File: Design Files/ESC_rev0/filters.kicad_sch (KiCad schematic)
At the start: 0 parts

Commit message: update 9
filters and USB complete
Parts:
- added C49, C50, C52, C54: 100n, symbol Device:C
- added C51, C53, C55, C58: 4n7, symbol Device:C
- added J9: Conn_01x06, symbol Connector_Generic:Conn_01x06
- added R45, R47, R49, R50: 10k, symbol Device:R
- added R46, R48, R52: 2k2, symbol Device:R
- added R51: 0R, symbol Device:R
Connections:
- new net +3.3V: C49.1, C50.1, C52.1, C54.1, R46.1, R48.1, R50.1, R52.1
- new net +5V: J9.6 (Pin_6)
- new net GND: C49.2, C50.2, C51.2, C52.2, C53.2, C54.2, C55.2, C58.2, J9.1 (Pin_1)
- new net HALL_1_IN: C58.1, J9.4 (Pin_4), R45.1, R52.2
- new net HALL_2_IN: C53.1, J9.3 (Pin_3), R48.2, R49.1
- new net HALL_3_IN: C51.1, J9.2 (Pin_2), R46.2, R47.1
- new net HALL_3_OUT: R45.2, R47.2, R49.2, R51.2
- new net TEMP_IN: C55.1, J9.5 (Pin_5), R50.2, R51.1
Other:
- note added: "${TITLE}"
- note added: "HALL_1 Filter"
- note added: "HALL_2 Filter"
- note added: "HALL_3 Filter"
- note added: "Hall Encoder Input"
- note added: "Hall Encoder Output to MCU"
- note added: "TEMP Filter"
- title: (none) -> FILTERS

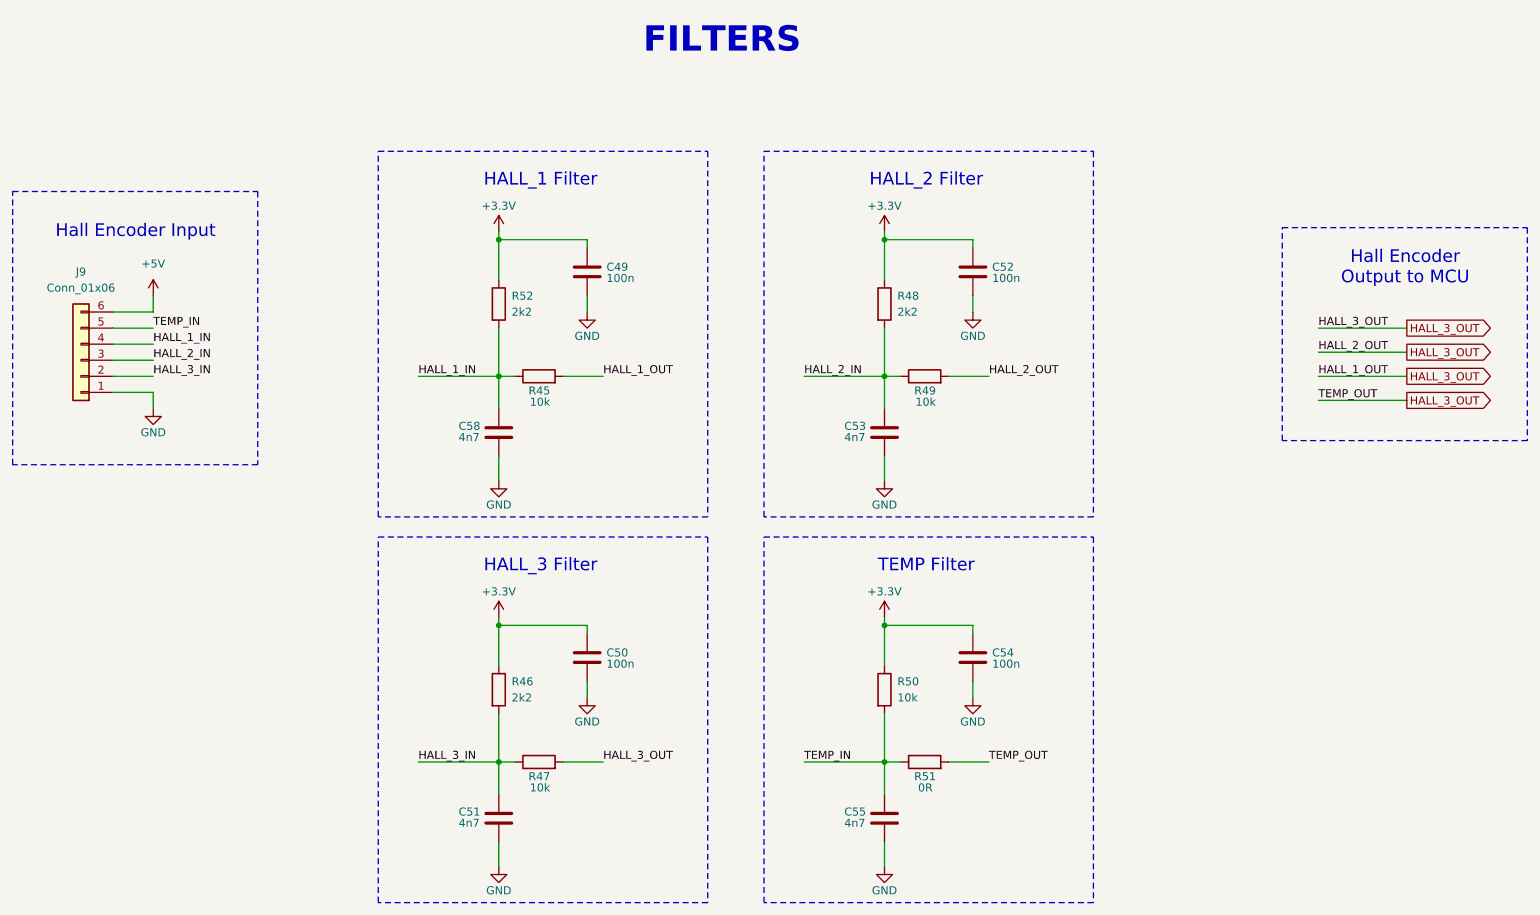
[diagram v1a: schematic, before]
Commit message: UPDATE 12
started schematics revision: edit and added info and circuits to some pages and assigned some footprints for components
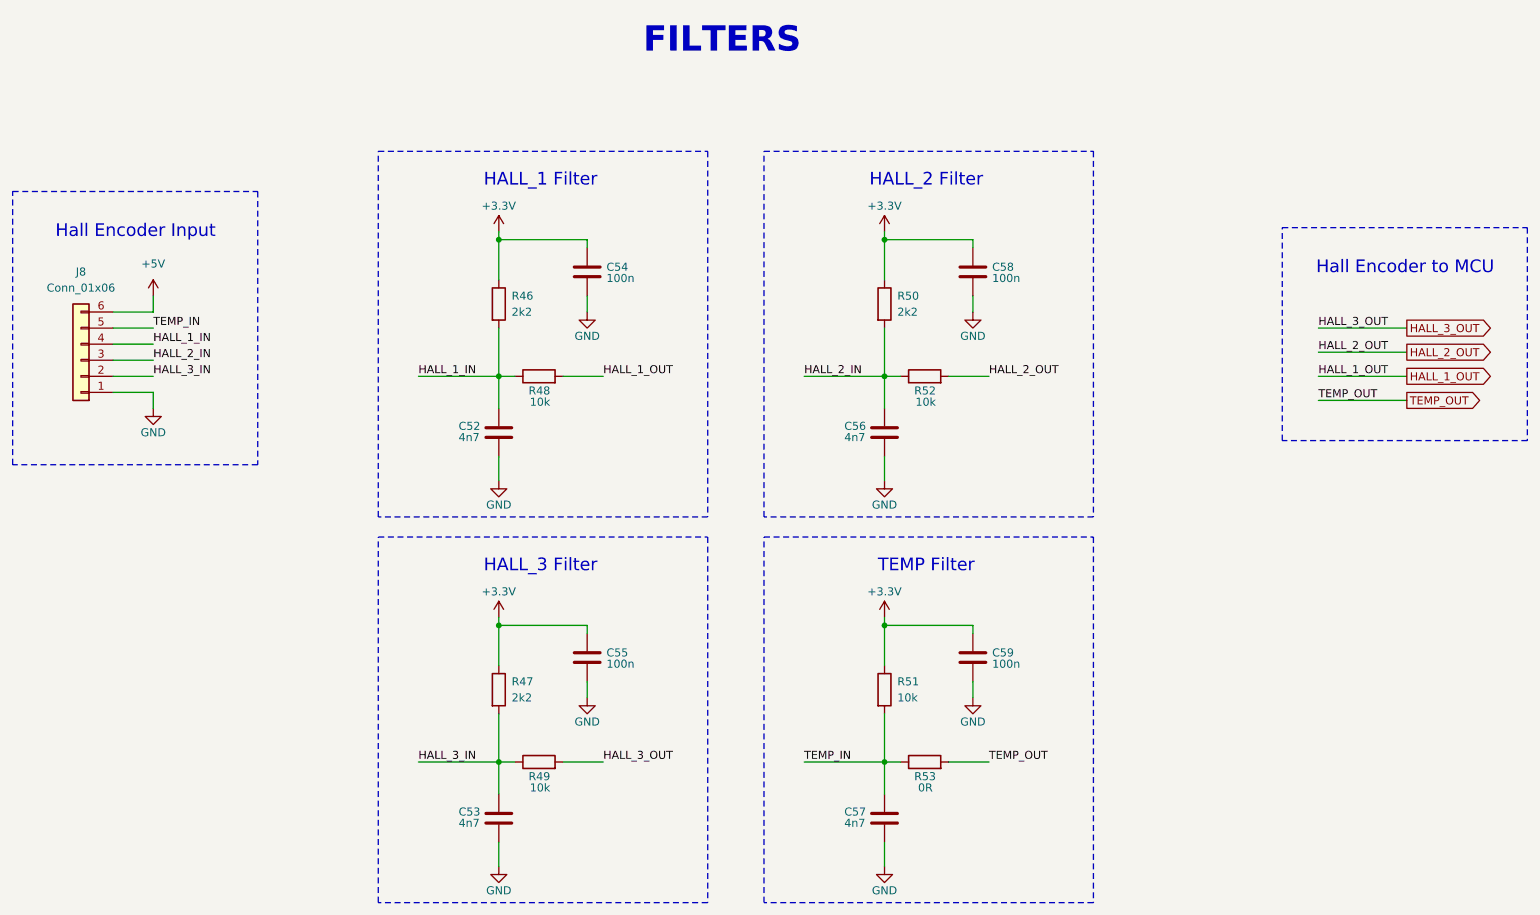
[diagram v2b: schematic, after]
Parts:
- C52: renamed from C58; footprint (none) -> Capacitor_SMD:C_0201_0603Metric
- C53: renamed from C51; footprint (none) -> Capacitor_SMD:C_0201_0603Metric
- C54: renamed from C49; footprint (none) -> Capacitor_SMD:C_0201_0603Metric
- C55: renamed from C50; footprint (none) -> Capacitor_SMD:C_0201_0603Metric
- C56: renamed from C53; footprint (none) -> Capacitor_SMD:C_0201_0603Metric
- C57: renamed from C55; footprint (none) -> Capacitor_SMD:C_0201_0603Metric
- C58: renamed from C52; footprint (none) -> Capacitor_SMD:C_0201_0603Metric
- C59: renamed from C54; footprint (none) -> Capacitor_SMD:C_0201_0603Metric
- renumbered J9 to J8, R52 to R46, R46 to R47, R45 to R48, R47 to R49, R48 to R50, R50 to R51, R49 to R52, R51 to R53
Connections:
- net HALL_3_OUT: no longer R48.2, R52.2, R53.2
- new net HALL_1_OUT: R48.2
- new net HALL_2_OUT: R52.2
- new net TEMP_OUT: R53.2
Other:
- note added: "Hall Encoder to MCU"
- note removed: "Hall Encoder Output to MCU"

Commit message: update 13
assigned all footprints (provisionally) and imported them - errors and warning occurred, must be corrected in the future
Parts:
- J8: footprint (none) -> Connector_PinHeader_2.00mm:PinHeader_1x06_P2.00mm_Vertical
- R46, R47, R48, R49, R50, R51, R52, R53: footprint (none) -> Resistor_SMD:R_0603_1608Metric
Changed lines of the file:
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@@
 			)
 		)
-		(property "Footprint" ""
+		(property "Footprint" "Resistor_SMD:R_0603_1608Metric"
 			(at 106.68 79.248 90)
 			(effects
@@
 			)
 		)
-		(property "Footprint" ""
+		(property "Footprint" "Resistor_SMD:R_0603_1608Metric"
 			(at 167.64 140.208 90)
 			(effects
@@
 			)
 		)
-		(property "Footprint" ""
+		(property "Footprint" "Resistor_SMD:R_0603_1608Metric"
 			(at 106.68 140.208 90)
 			(effects
@@
 			)
 		)
-		(property "Footprint" ""
+		(property "Footprint" "Resistor_SMD:R_0603_1608Metric"
 			(at 98.552 127 90)
 			(effects
@@
 			)
 		)
-		(property "Footprint" ""
+		(property "Footprint" "Resistor_SMD:R_0603_1608Metric"
 			(at 159.512 66.04 90)
 			(effects
@@
 			)
 		)
-		(property "Footprint" ""
+		(property "Footprint" "Resistor_SMD:R_0603_1608Metric"
 			(at 98.552 66.04 90)
 			(effects
@@
 			)
 		)
-		(property "Footprint" ""
+		(property "Footprint" "Resistor_SMD:R_0603_1608Metric"
 			(at 159.512 127 90)
 			(effects
@@
 			)
 		)
-		(property "Footprint" ""
+		(property "Footprint" "Connector_PinHeader_2.00mm:PinHeader_1x06_P2.00mm_Vertical"
 			(at 34.29 74.93 0)
 			(effects
@@
 			)
 		)
-		(property "Footprint" ""
+		(property "Footprint" "Resistor_SMD:R_0603_1608Metric"
 			(at 167.64 79.248 90)
 			(effects

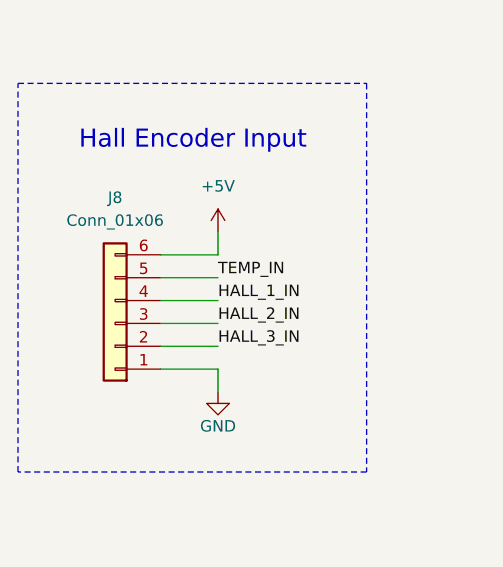
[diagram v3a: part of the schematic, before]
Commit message: update 15
Simple connectors replaced by smd connectors (downloaded). Connectors were placed in edges of the board.
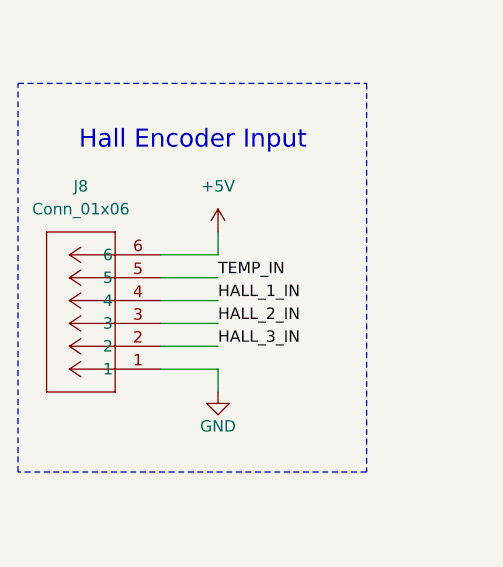
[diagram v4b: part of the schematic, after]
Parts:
- J8: footprint Connector_PinHeader_2.00mm:PinHeader_1x06_P2.00mm_Vertical -> CONN_S6B-XH-SM4-TB_JST; symbol Connector_Generic:Conn_01x06 -> S6B-XH-SM4-TB:S6B-XH-SM4-TB
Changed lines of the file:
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@@
 	)
 	(symbol
-		(lib_id "Connector_Generic:Conn_01x06")
-		(at 34.29 74.93 180)
+		(lib_id "S6B-XH-SM4-TB:S6B-XH-SM4-TB")
+		(at 39.37 80.01 180)
 		(unit 1)
 		(exclude_from_sim no)
@@
 		(fields_autoplaced yes)
 		(property "Reference" "J8"
-			(at 34.29 60.96 0)
+			(at 30.48 59.69 0)
 			(effects
 				(font
@@
 		)
 		(property "Value" "Conn_01x06"
-			(at 34.29 63.5 0)
+			(at 30.48 62.23 0)
 			(effects
 				(font
@@
 			)
 		)
-		(property "Footprint" "Connector_PinHeader_2.00mm:PinHeader_1x06_P2.00mm_Vertical"
-			(at 34.29 74.93 0)
+		(property "Footprint" "CONN_S6B-XH-SM4-TB_JST"
+			(at 36.068 63.246 0)
 			(effects
 				(font
 					(size 1.27 1.27)
+					(italic yes)
 				)
 				(hide yes)
 			)
 		)
-		(property "Datasheet" "~"
-			(at 34.29 74.93 0)
+		(property "Datasheet" "S6B-XH-SM4-TB"
+			(at 41.656 83.566 0)
 			(effects
 				(font
 					(size 1.27 1.27)
+					(italic yes)
 				)
 				(hide yes)
@@
 		)
 		(property "Description" "Generic connector, single row, 01x06, script generated (kicad-library-utils/schlib/autogen/connector/)"
-			(at 34.29 74.93 0)
+			(at 39.37 80.01 0)
 			(effects
 				(font

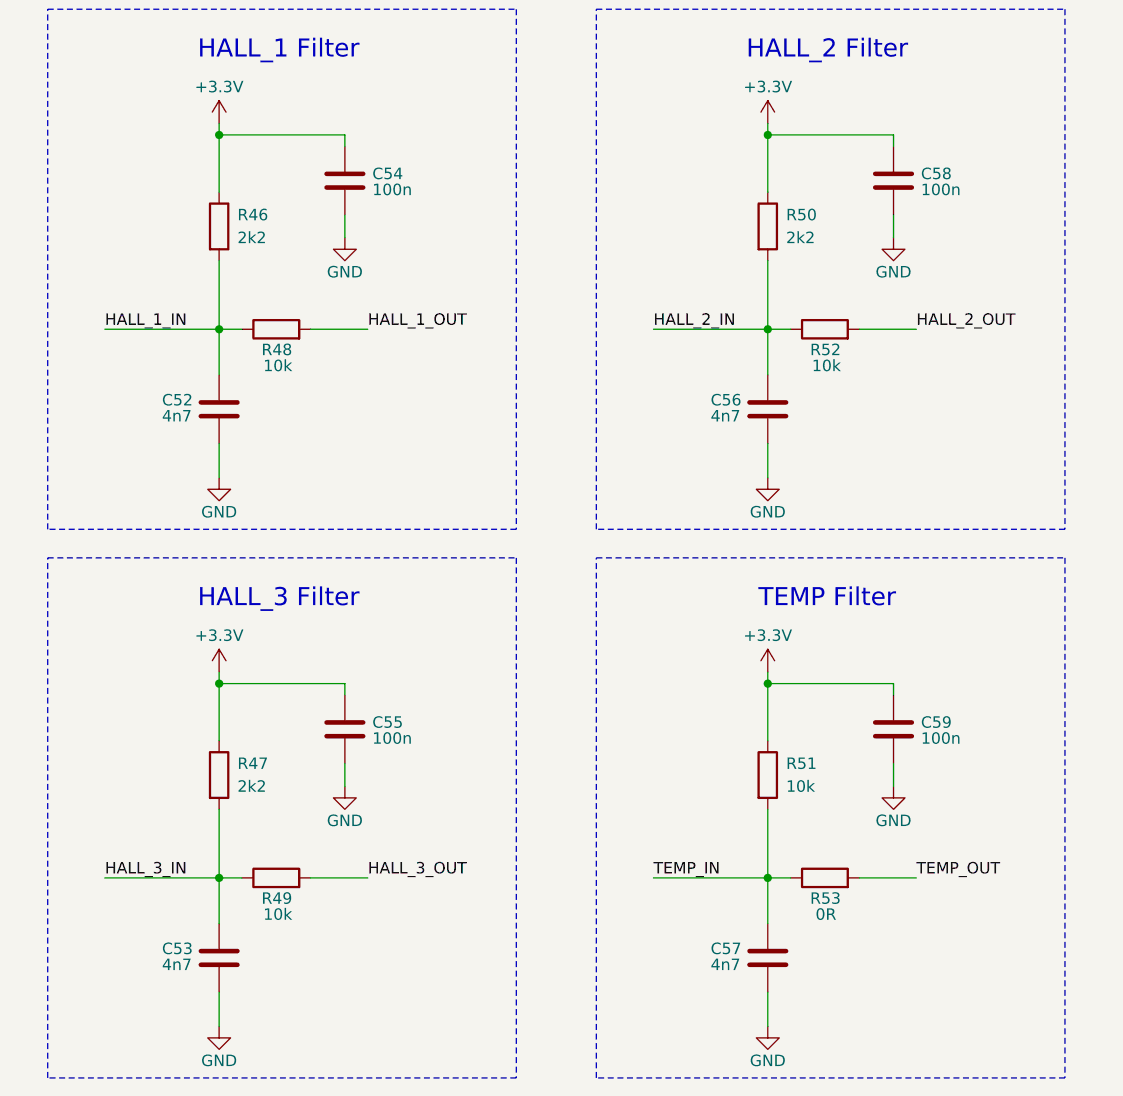
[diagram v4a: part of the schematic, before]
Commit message: update 16
All components placed on board. Some components modifications and addition were made: added 3D models, changed some symbols and footprints positions and some component types.
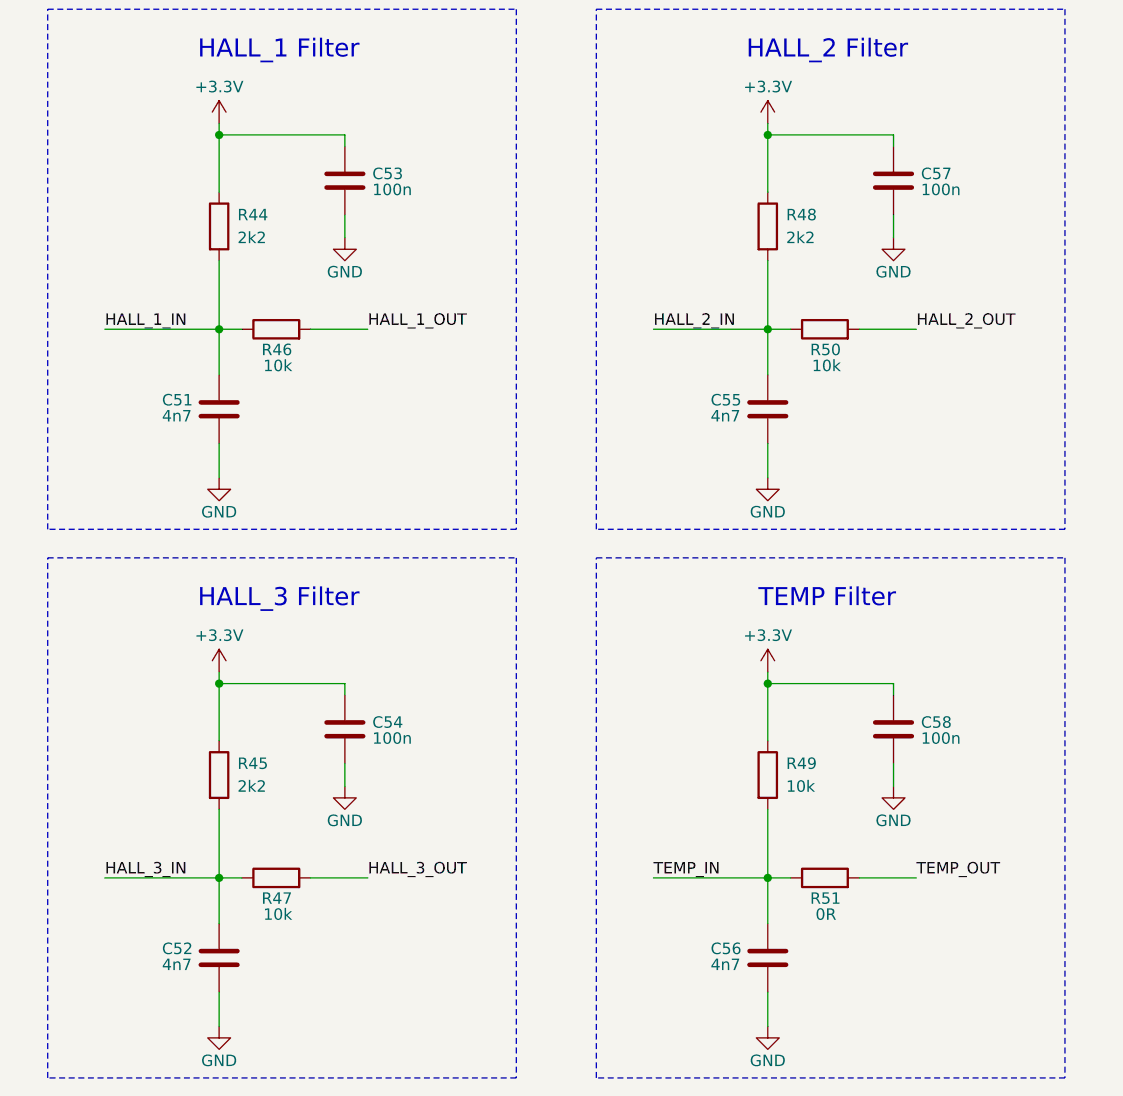
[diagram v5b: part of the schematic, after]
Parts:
- C51: renamed from C52; footprint Capacitor_SMD:C_0201_0603Metric -> Capacitor_SMD:C_0603_1608Metric
- C52: renamed from C53; footprint Capacitor_SMD:C_0201_0603Metric -> Capacitor_SMD:C_0603_1608Metric
- C53: renamed from C54; footprint Capacitor_SMD:C_0201_0603Metric -> Capacitor_SMD:C_0603_1608Metric
- C54: renamed from C55; footprint Capacitor_SMD:C_0201_0603Metric -> Capacitor_SMD:C_0603_1608Metric
- C55: renamed from C56; footprint Capacitor_SMD:C_0201_0603Metric -> Capacitor_SMD:C_0603_1608Metric
- C56: renamed from C57; footprint Capacitor_SMD:C_0201_0603Metric -> Capacitor_SMD:C_0603_1608Metric
- C57: renamed from C58; footprint Capacitor_SMD:C_0201_0603Metric -> Capacitor_SMD:C_0603_1608Metric
- C58: renamed from C59; footprint Capacitor_SMD:C_0201_0603Metric -> Capacitor_SMD:C_0603_1608Metric
- J8: footprint CONN_S6B-XH-SM4-TB_JST -> S6B-XH-SM4-TB:CONN_S6B-XH-SM4-TB_JST
- renumbered R46 to R44, R47 to R45, R48 to R46, R49 to R47, R50 to R48, R51 to R49, R52 to R50, R53 to R51

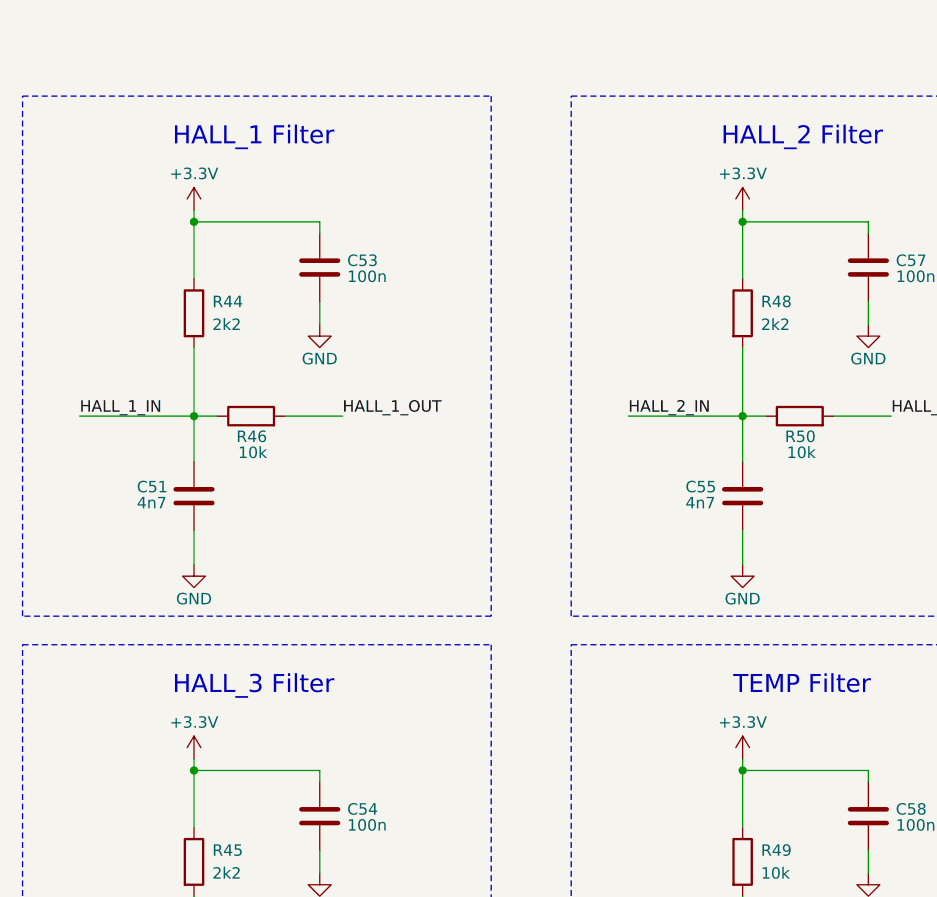
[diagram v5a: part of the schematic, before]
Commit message: update 18
Route process partially complete. Some corrections were made in footprints and pins references. Probably the power lines will need changes in size.
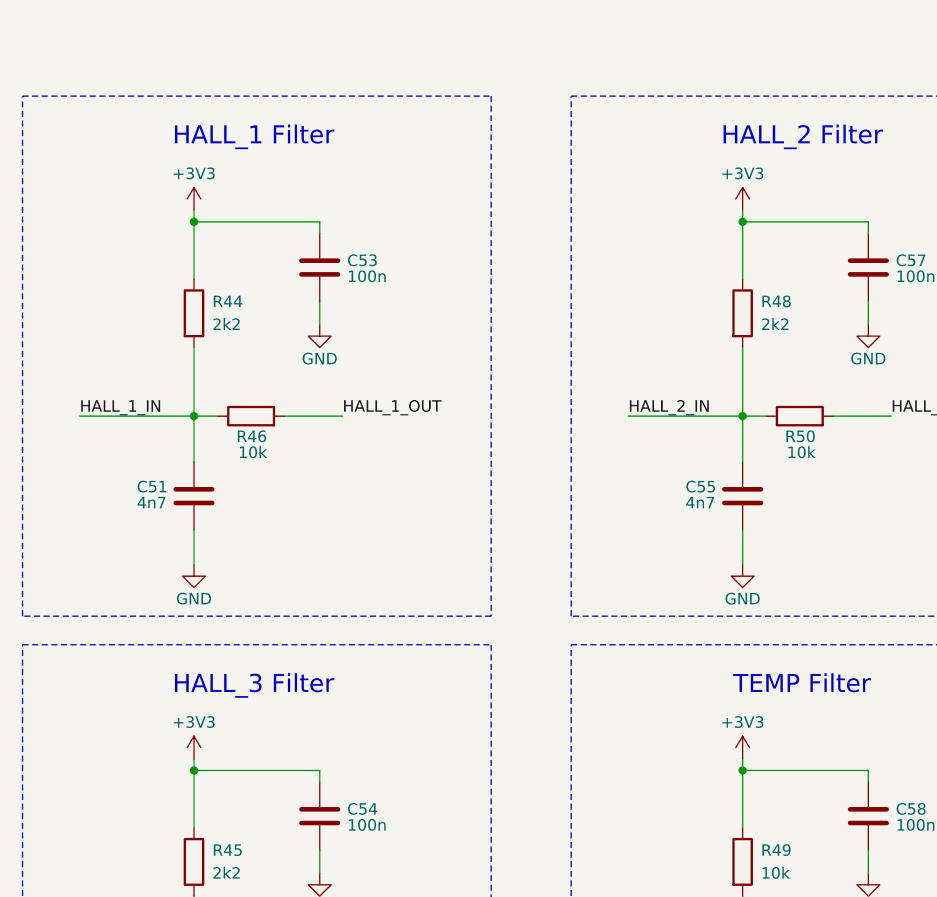
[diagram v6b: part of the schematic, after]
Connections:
- net +3.3V renamed +3V3
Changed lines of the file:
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@@
 			)
 		)
-		(property "Value" "+3.3V"
+		(property "Value" "+3V3"
 			(at 100.33 50.546 0)
 			(effects
@@
 			)
 		)
-		(property "Value" "+3.3V"
+		(property "Value" "+3V3"
 			(at 161.29 111.506 0)
 			(effects
@@
 			)
 		)
-		(property "Value" "+3.3V"
+		(property "Value" "+3V3"
 			(at 100.33 111.506 0)
 			(effects
@@
 			)
 		)
-		(property "Value" "+3.3V"
+		(property "Value" "+3V3"
 			(at 161.29 50.546 0)
 			(effects
